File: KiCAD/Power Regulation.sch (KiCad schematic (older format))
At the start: 0 parts

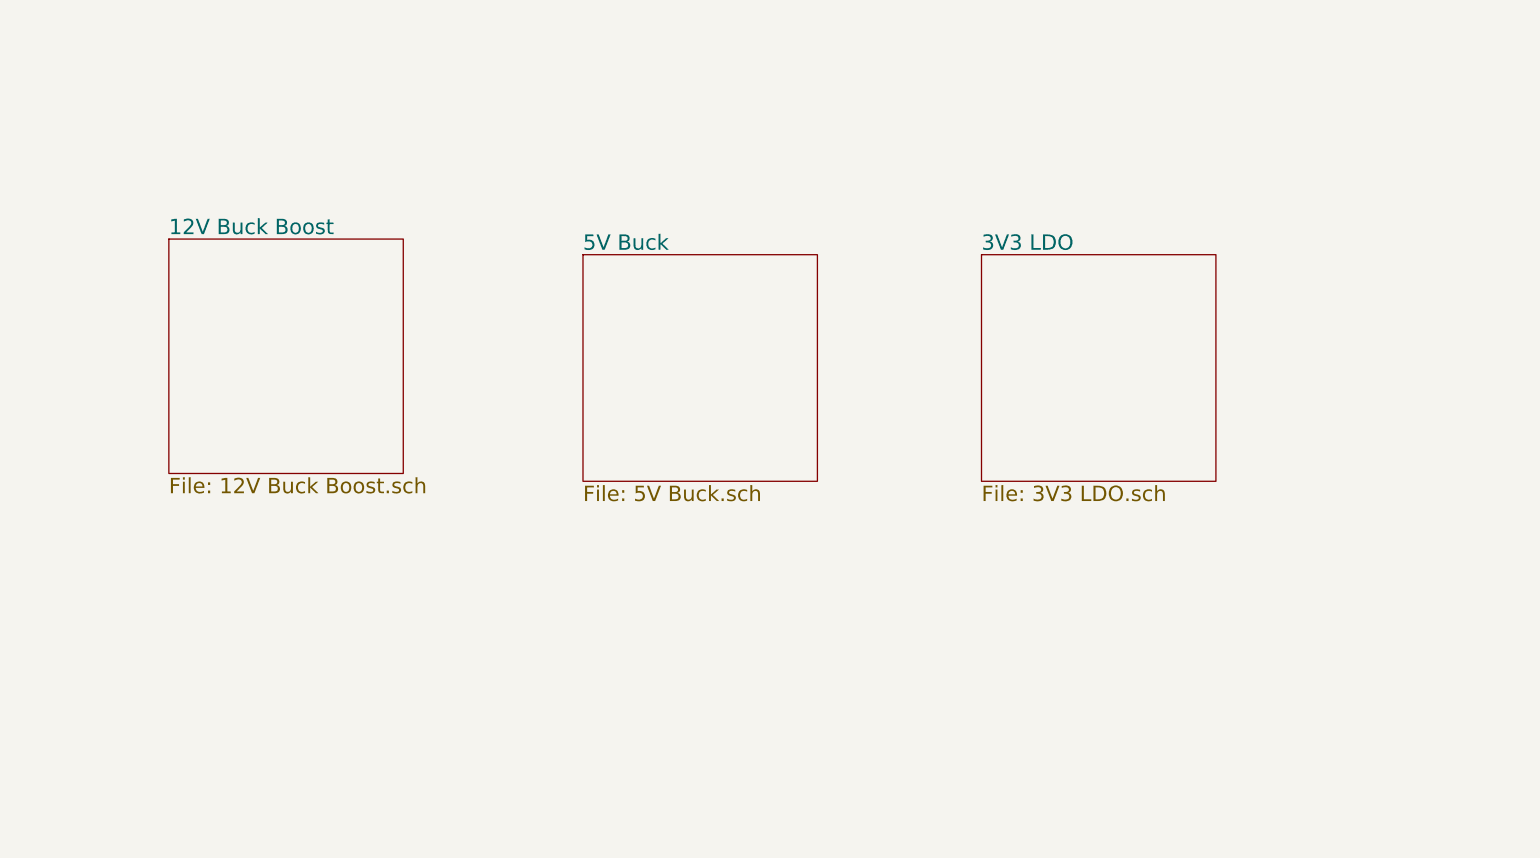
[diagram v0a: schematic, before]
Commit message: completed 5V buck schematic and setup
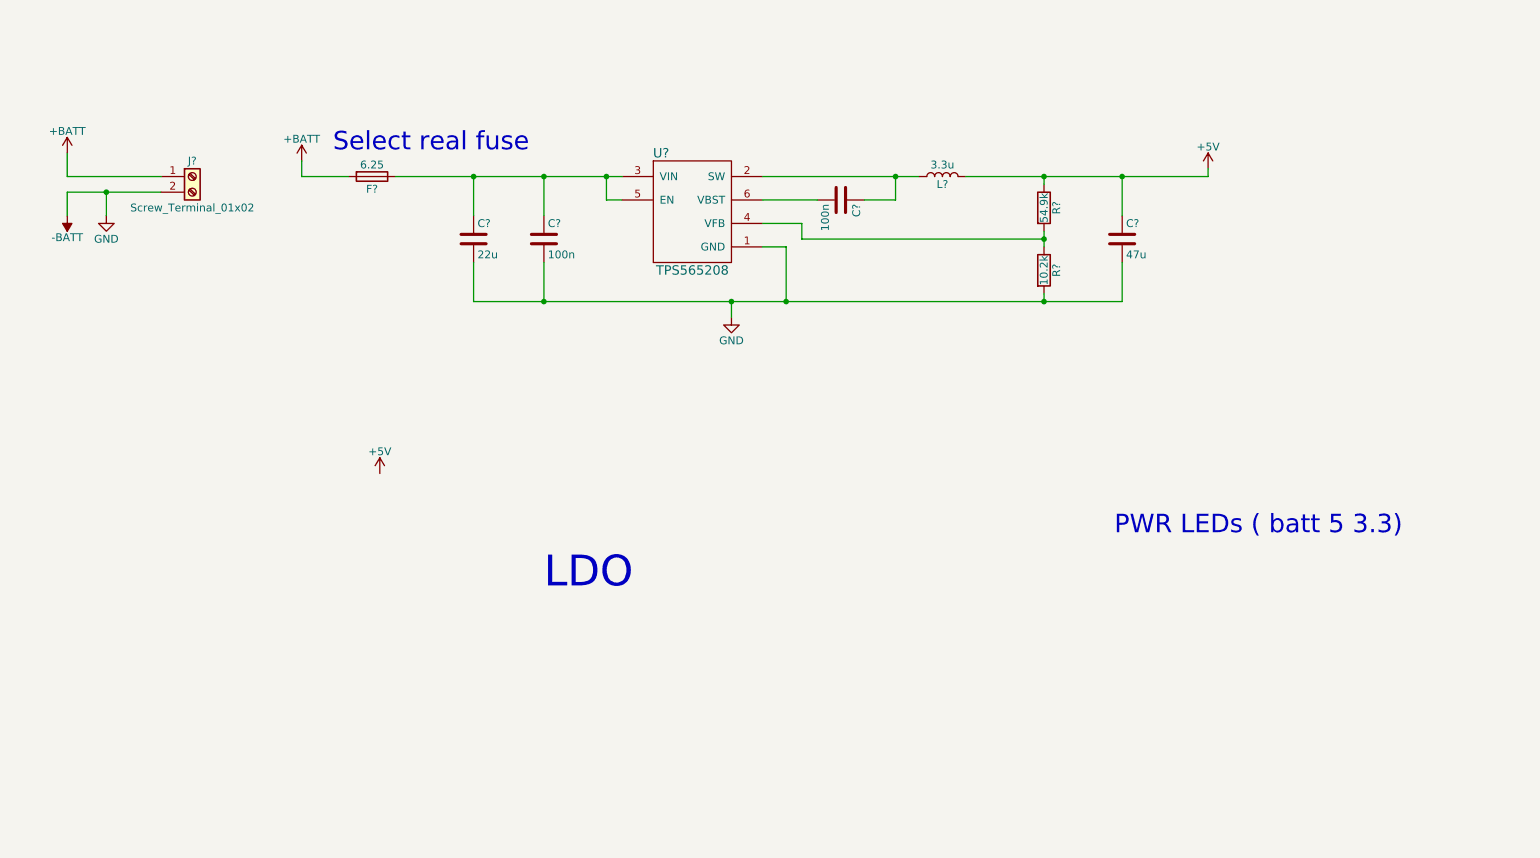
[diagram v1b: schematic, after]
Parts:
- added C?: 22u, Capacitors_SMD:C_1210, symbol C
- added C? (x2): 100n, Capacitors_SMD:C_0603, symbol C
- added C?: 47u, Capacitors_SMD:C_1206, symbol C
- added F?: 6.25, Fuse_Holders_and_Fuses:Fuseholder5x20_horiz_open_lateral_Type-II, symbol Fuse
- added J?: Screw_Terminal_01x02, TerminalBlock:TerminalBlock_bornier-2_P5.08mm, symbol Screw_Terminal_01x02
- added L?: 3.3u, footprints:XAL7030, symbol L
- added R?: 10.2k, Resistors_SMD:R_0402, symbol R
- added R?: 54.9k, Resistors_SMD:R_0402, symbol R
- added U?: TPS565208, TO_SOT_Packages_SMD:TSOT-23-6, symbol TPS565208
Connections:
- new net: C?.1, L?.1, U?.2 (SW)
- new net: C?.1, C?.1, F?.1, U?.3 (VIN), U?.5 (EN)
- new net: R?.1, R?.2, U?.4 (VFB)
- new net: C?.2, U?.6 (VBST)
- new net +5V: C?.1, L?.2, R?.1
- new net +BATT: F?.2, J?.1 (Pin_1)
- new net -BATT: C?.2, C?.2, C?.2, J?.2 (Pin_2), R?.2, U?.1 (GND)
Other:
- note added: "LDO"
- note added: "PWR LEDs ( batt 5 3.3)"
- note added: "Select real fuse"

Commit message: µC ATMEGA2560 added and pins labeled, w/ supp components
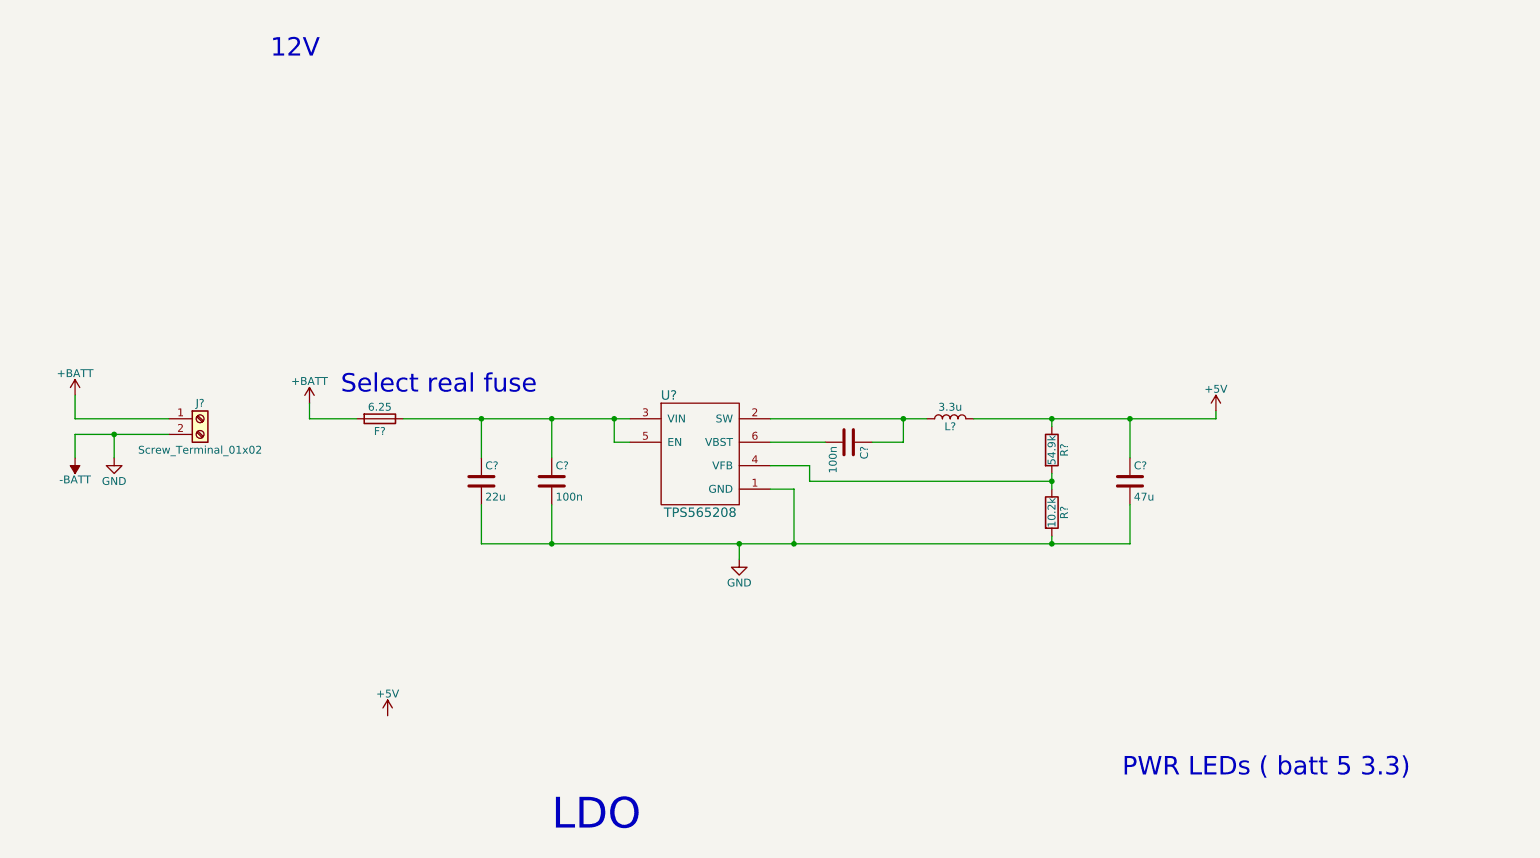
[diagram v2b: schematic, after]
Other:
- note added: "12V\n"
- moved on the sheet: C?, F?, J?, L?, R?, U?

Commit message: Schematic small fix
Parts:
- added C1: 10u, Capacitors_SMD:C_1210, symbol C
- added C2: 22u, Capacitors_SMD:C_1210, symbol C
- added D1, D2, D3: LED, LEDs:LED_0805, symbol LED
- added R3: 390, Resistors_SMD:R_0805, symbol R
- added R4: 110, Resistors_SMD:R_0805, symbol R
- added R5: 43, Resistors_SMD:R_0805, symbol R
- added U1: AP1117-33, TO_SOT_Packages_SMD:SOT-223-3Lead_TabPin2, symbol AP1117-33
- gave numbers to parts that had none: 10
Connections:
- net +5V: now also C1.1, D2.2 (A), U1.3 (VI)
- net -BATT: now also C1.2, C2.2, R3.1, R4.1, R5.1, U1.1 (GND)
- net +BATT renamed +12V
- net +12V: now also D1.2 (A)
- new net: D1.1 (K), R3.2
- new net: D2.1 (K), R4.2
- new net: D3.1 (K), R5.2
- new net +3V3: C2.1, D3.2 (A), U1.2 (VO)
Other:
- note added: "3V3"
- note added: "5V"
- note added: "PWR Indication"
- note added: "Supplied from Lead Acid Battery"
- note removed: "PWR LEDs ( batt 5 3.3)"
- moved on the sheet: C3, C4, C5, C6, F1, J1, L1, R1, R2, U2

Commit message: transfer for mechanical step
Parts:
- removed U1: AP1117-33, TO_SOT_Packages_SMD:SOT-223-3Lead_TabPin2, symbol AP1117-33
- added C30: 10n, Capacitors_SMD:C_0805, symbol C
- added D7: D, Resistors_THT:R_Axial_DIN0204_L3.6mm_D1.6mm_P5.08mm_Horizontal, symbol D
- added U1: LP2985-3.3, TO_SOT_Packages_SMD:SOT-23-5, symbol LP2985-3.3
- C1, C2: footprint Capacitors_SMD:C_1210 -> Capacitors_SMD:C_0805
- F1: footprint Fuse_Holders_and_Fuses:Fuseholder5x20_horiz_open_lateral_Type-II -> (none)
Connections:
- net +12V: now also C3.1, C4.1, F1.1, U2.3 (VIN), U2.5 (EN), D7.2 (A)
- net +3V3: now also U1.5 (VOUT)
- net +5V: now also U1.1 (VIN), U1.3 (ON/~OFF~)
- net -BATT: now also C30.2, D7.1 (K), U1.2 (GND)
- new net: C30.1, U1.4 (BP)
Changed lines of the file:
@@
 $EndComp
 $Comp
-L +BATT #PWR01
+L +BATT #PWR1
 U 1 1 5A90FE91
 P 1550 2100
-F 0 "#PWR01" H 1550 1950 50  0001 C CNN
+F 0 "#PWR1" H 1550 1950 50  0001 C CNN
 F 1 "+BATT" H 1550 2240 50  0000 C CNN
 F 2 "" H 1550 2100 50  0001 C CNN
@@
 $EndComp
 $Comp
-L -BATT #PWR02
+L -BATT #PWR2
 U 1 1 5A90FEBB
 P 1550 2500
-F 0 "#PWR02" H 1550 2350 50  0001 C CNN
+F 0 "#PWR2" H 1550 2350 50  0001 C CNN
 F 1 "-BATT" H 1550 2640 50  0000 C CNN
 F 2 "" H 1550 2500 50  0001 C CNN
@@
 $EndComp
 $Comp
-L GND #PWR03
+L GND #PWR3
 U 1 1 5A90FFB1
 P 1800 2500
-F 0 "#PWR03" H 1800 2250 50  0001 C CNN
+F 0 "#PWR3" H 1800 2250 50  0001 C CNN
 F 1 "GND" H 1800 2350 50  0000 C CNN
 F 2 "" H 1800 2500 50  0001 C CNN
@@
 $EndComp
 $Comp
-L +BATT #PWR04
+L +BATT #PWR9
 U 1 1 5A910014
 P 3050 2150
-F 0 "#PWR04" H 3050 2000 50  0001 C CNN
+F 0 "#PWR9" H 3050 2000 50  0001 C CNN
 F 1 "+BATT" H 3050 2290 50  0000 C CNN
 F 2 "" H 3050 2150 50  0001 C CNN
@@
 $EndComp
 $Comp
-L GND #PWR05
+L GND #PWR13
 U 1 1 5A9102A0
 P 5800 3150
-F 0 "#PWR05" H 5800 2900 50  0001 C CNN
+F 0 "#PWR13" H 5800 2900 50  0001 C CNN
 F 1 "GND" H 5800 3000 50  0000 C CNN
 F 2 "" H 5800 3150 50  0001 C CNN
@@
 Connection ~ 7800 3050
 $Comp
-L +5V #PWR06
+L +5V #PWR14
 U 1 1 5A9107CF
 P 8850 2200
-F 0 "#PWR06" H 8850 2050 50  0001 C CNN
+F 0 "#PWR14" H 8850 2050 50  0001 C CNN
 F 1 "+5V" H 8850 2340 50  0000 C CNN
 F 2 "" H 8850 2200 50  0001 C CNN
@@
 $EndComp
 $Comp
-L +5V #PWR07
+L +5V #PWR4
 U 1 1 5A9114DE
 P 1950 4350
-F 0 "#PWR07" H 1950 4200 50  0001 C CNN
+F 0 "#PWR4" H 1950 4200 50  0001 C CNN
 F 1 "+5V" H 1950 4490 50  0000 C CNN
 F 2 "" H 1950 4350 50  0001 C CNN
@@
 F 0 "F1" V 3580 2250 50  0000 C CNN
 F 1 "6.25" V 3425 2250 50  0000 C CNN
-F 2 "Fuse_Holders_and_Fuses:Fuseholder5x20_horiz_open_lateral_Type-II" V 3430 2250 50  0001 C CNN
+F 2 "" V 3430 2250 50  0001 C CNN
 F 3 "" H 3500 2250 50  0001 C CNN
 	1    3500 2250
@@
 $EndComp
 $Comp
-L GND #PWR08
+L GND #PWR18
 U 1 1 5AE1251F
 P 10850 4800
-F 0 "#PWR08" H 10850 4550 50  0001 C CNN
+F 0 "#PWR18" H 10850 4550 50  0001 C CNN
 F 1 "GND" H 10850 4650 50  0000 C CNN
 F 2 "" H 10850 4800 50  0001 C CNN
@@
 	9950 4600 10100 4600
 $Comp
-L +BATT #PWR09
+L +BATT #PWR6
 U 1 1 5AE127EB
 P 2150 1200
-F 0 "#PWR09" H 2150 1050 50  0001 C CNN
+F 0 "#PWR6" H 2150 1050 50  0001 C CNN
 F 1 "+BATT" H 2150 1340 50  0000 C CNN
 F 2 "" H 2150 1200 50  0001 C CNN
@@
 $EndComp
 $Comp
-L +12V #PWR010
+L +12V #PWR7
 U 1 1 5AE12828
 P 2500 1200
-F 0 "#PWR010" H 2500 1050 50  0001 C CNN
+F 0 "#PWR7" H 2500 1050 50  0001 C CNN
 F 1 "+12V" H 2500 1340 50  0000 C CNN
 F 2 "" H 2500 1200 50  0001 C CNN
@@
 	2500 1250 2500 1200
 $Comp
-L +12V #PWR011
+L +12V #PWR17
 U 1 1 5AE132B3
 P 9400 3850
-F 0 "#PWR011" H 9400 3700 50  0001 C CNN
+F 0 "#PWR17" H 9400 3700 50  0001 C CNN
 F 1 "+12V" H 9400 3990 50  0000 C CNN
 F 2 "" H 9400 3850 50  0001 C CNN
@@
 $EndComp
 $Comp
-L +5V #PWR012
+L +5V #PWR16
 U 1 1 5AE132EE
 P 9200 3850
-F 0 "#PWR012" H 9200 3700 50  0001 C CNN
+F 0 "#PWR16" H 9200 3700 50  0001 C CNN
 F 1 "+5V" H 9200 3990 50  0000 C CNN
 F 2 "" H 9200 3850 50  0001 C CNN
@@
 $EndComp
 $Comp
-L +3V3 #PWR013
+L +3V3 #PWR15
 U 1 1 5AE1333B
 P 9000 3850
-F 0 "#PWR013" H 9000 3700 50  0001 C CNN
+F 0 "#PWR15" H 9000 3700 50  0001 C CNN
 F 1 "+3V3" H 9000 3990 50  0000 C CNN
 F 2 "" H 9000 3850 50  0001 C CNN
@@
 Wire Wire Line
 	9000 4600 9650 4600
-$Comp
-L AP1117-33 U1
-U 1 1 5AE94400
-P 2700 4550
-F 0 "U1" H 2550 4675 50  0000 C CNN
-F 1 "AP1117-33" H 2700 4675 50  0000 L CNN
-F 2 "TO_SOT_Packages_SMD:SOT-223-3Lead_TabPin2" H 2700 4750 50  0001 C CNN
-F 3 "" H 2800 4300 50  0001 C CNN
-	1    2700 4550
-	1    0    0    -1
-$EndComp
 Wire Wire Line
 	1950 4350 1950 4550
 Wire Wire Line
-	1950 4550 2400 4550
-$Comp
-L +3V3 #PWR014
+	1950 4550 2300 4550
+$Comp
+L +3V3 #PWR12
 U 1 1 5AE94636
 P 3500 4350
-F 0 "#PWR014" H 3500 4200 50  0001 C CNN
+F 0 "#PWR12" H 3500 4200 50  0001 C CNN
 F 1 "+3V3" H 3500 4490 50  0000 C CNN
 F 2 "" H 3500 4350 50  0001 C CNN
@@
 	3500 4550 3500 4350
 Wire Wire Line
-	3000 4550 3500 4550
-$Comp
-L GND #PWR015
+	3100 4550 3500 4550
+$Comp
+L GND #PWR8
 U 1 1 5AE94712
 P 2700 5050
-F 0 "#PWR015" H 2700 4800 50  0001 C CNN
+F 0 "#PWR8" H 2700 4800 50  0001 C CNN
 F 1 "GND" H 2700 4900 50  0000 C CNN
 F 2 "" H 2700 5050 50  0001 C CNN
@@
 $EndComp
 Wire Wire Line
-	2700 5050 2700 4850
+	2700 4950 2700 5050
 $Comp
 L C C1
@@
 F 0 "C1" H 2125 4900 50  0000 L CNN
 F 1 "10u" H 2125 4700 50  0000 L CNN
-F 2 "Capacitors_SMD:C_1210" H 2138 4650 50  0001 C CNN
+F 2 "Capacitors_SMD:C_0805" H 2138 4650 50  0001 C CNN
 F 3 "" H 2100 4800 50  0001 C CNN
 F 4 "2m" H 2100 4800 60  0001 C CNN "ESR"
@@
 F 0 "C2" H 3325 4900 50  0000 L CNN
 F 1 "22u" H 3325 4700 50  0000 L CNN
-F 2 "Capacitors_SMD:C_1210" H 3338 4650 50  0001 C CNN
+F 2 "Capacitors_SMD:C_0805" H 3338 4650 50  0001 C CNN
 F 3 "" H 3300 4800 50  0001 C CNN
 F 4 "2m" H 3300 4800 60  0001 C CNN "ESR"
@@
 $EndComp
 $Comp
-L GND #PWR016
+L GND #PWR5
 U 1 1 5AE94AA0
 P 2100 5050
-F 0 "#PWR016" H 2100 4800 50  0001 C CNN
+F 0 "#PWR5" H 2100 4800 50  0001 C CNN
 F 1 "GND" H 2100 4900 50  0000 C CNN
 F 2 "" H 2100 5050 50  0001 C CNN
@@
 $EndComp
 $Comp
-L GND #PWR017
+L GND #PWR11
 U 1 1 5AE94AE4
 P 3300 5050
-F 0 "#PWR017" H 3300 4800 50  0001 C CNN
+F 0 "#PWR11" H 3300 4800 50  0001 C CNN
 F 1 "GND" H 3300 4900 50  0000 C CNN
 F 2 "" H 3300 5050 50  0001 C CNN
@@
 Wire Wire Line
 	2100 4950 2100 5050
+$Comp
+L LP2985-3.3 U1
+U 1 1 5AEEF302
+P 2700 4650
+F 0 "U1" H 2450 4875 50  0000 C CNN
+F 1 "LP2985-3.3" H 2700 4875 50  0000 L CNN
+F 2 "TO_SOT_Packages_SMD:SOT-23-5" H 2700 4975 50  0001 C CNN
+F 3 "" H 2700 4650 50  0001 C CNN
+	1    2700 4650
+	1    0    0    -1
+$EndComp
+$Comp
+L C C30
+U 1 1 5AEEF5D4
+P 3100 4800
+F 0 "C30" H 3125 4900 50  0000 L CNN
+F 1 "10n" H 3125 4700 50  0000 L CNN
+F 2 "Capacitors_SMD:C_0805" H 3138 4650 50  0001 C CNN
+F 3 "" H 3100 4800 50  0001 C CNN
+F 4 "2m" H 3100 4800 60  0001 C CNN "ESR"
+F 5 "25" H 3100 4800 60  0001 C CNN "VDC"
+	1    3100 4800
+	1    0    0    -1
+$EndComp
+$Comp
+L GND #PWR10
+U 1 1 5AEEF62A
+P 3100 5050
+F 0 "#PWR10" H 3100 4800 50  0001 C CNN
+F 1 "GND" H 3100 4900 50  0000 C CNN
+F 2 "" H 3100 5050 50  0001 C CNN
+F 3 "" H 3100 5050 50  0001 C CNN
+	1    3100 5050
+	1    0    0    -1
+$EndComp
+Wire Wire Line
+	3100 5050 3100 4950
+Wire Wire Line
+	2300 4650 2200 4650
+Wire Wire Line
+	2200 4650 2200 4550
+Connection ~ 2200 4550
+Wire Wire Line
+	3350 2250 3350 2450
+Wire Wire Line
+	3350 2450 3650 2450
+Wire Wire Line
+	3650 2450 3650 2250
+$Comp
+L D D7
+U 1 1 5AF1C272
+P 1400 2300
+F 0 "D7" H 1400 2400 50  0000 C CNN
+F 1 "D" H 1400 2200 50  0000 C CNN
+F 2 "Resistors_THT:R_Axial_DIN0204_L3.6mm_D1.6mm_P5.08mm_Horizontal" H 1400 2300 50  0001 C CNN
+F 3 "" H 1400 2300 50  0001 C CNN
+	1    1400 2300
+	0    -1   -1   0
+$EndComp
+Wire Wire Line
+	1550 2450 1400 2450
+Connection ~ 1550 2450
+Wire Wire Line
+	1400 2150 1550 2150
+Connection ~ 1550 2150
 $EndSCHEMATC

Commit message: fixed diode
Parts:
- removed D7: D, Resistors_THT:R_Axial_DIN0204_L3.6mm_D1.6mm_P5.08mm_Horizontal, symbol D
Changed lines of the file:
@@
 Wire Wire Line
 	3650 2450 3650 2250
-$Comp
-L D D7
-U 1 1 5AF1C272
-P 1400 2300
-F 0 "D7" H 1400 2400 50  0000 C CNN
-F 1 "D" H 1400 2200 50  0000 C CNN
-F 2 "Resistors_THT:R_Axial_DIN0204_L3.6mm_D1.6mm_P5.08mm_Horizontal" H 1400 2300 50  0001 C CNN
-F 3 "" H 1400 2300 50  0001 C CNN
-	1    1400 2300
-	0    -1   -1   0
-$EndComp
-Wire Wire Line
-	1550 2450 1400 2450
 Connection ~ 1550 2450
-Wire Wire Line
-	1400 2150 1550 2150
 Connection ~ 1550 2150
 $EndSCHEMATC
